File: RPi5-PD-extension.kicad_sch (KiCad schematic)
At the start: 4 parts, among them J1 HDMI0_Plug, J2 HDMI0_Receptacle, J3 HDMI1_Plug, J4 HDMI1_Receptacle

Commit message: Design v1
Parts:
- added C1, C13, C2: 10uF, symbol Device:C
- added C10, C7, C8, C9: 10nF, symbol Device:C
- added C11, C12, C21, C22, C23, C24, C25, C27, C28: 22uF, symbol Device:C
- added C14, C15, C29: 1uF, symbol Device:C
- added C16, C17, C3, C4: 330pF, symbol Device:C
- added C18, C20, C26: 100nF, symbol Device:C
- added C19: 22nF, symbol Device:C
- added C5, C6: 4.7uF, symbol Device:C
- added D1: BZT52C18, Diode_SMD:D_SOD-123F, symbol Diode:BZT52Bxx
- added J5: USB_C_PD_Receptacle, symbol Connector:USB_C_Receptacle_PowerOnly_6P
- added L1: 2.2uH, symbol Device:L
- added P1: USB_C_5V5A_Plug, symbol Connector:USB_C_Receptacle_USB2.0_14P
- added Q1: XR100P04, Package_TO_SOT_SMD:TO-252-2, symbol Transistor_FET:SUD50P04-08
- added R1, R2, R3, R5, R6: 10k, symbol Device:R
- added R10, R4: 220k, symbol Device:R
- added R11: 30k, symbol Device:R
- added R12: 330k, symbol Device:R
- added R13, R14, R7: 51k, symbol Device:R
- added R15: 1k, symbol Device:R
- added R8: 10m 1%, symbol Device:R
- added R9: 0, symbol Device:R
- added TP1: SWC, symbol Connector:TestPoint
- added TP2: GND, symbol Connector:TestPoint
- added TP3: VDD, symbol Connector:TestPoint
- added TP4: SWD, symbol Connector:TestPoint
- added U1: TPS25730D, Package_DFN_QFN:Texas_REF0038A_WQFN-38-2EP_6x4mm_P0.4, symbol Interface_USB:TPS25730D
- added U2: CYPD3175-24LQXQ, Package_DFN_QFN:QFN-24-1EP_4x4mm_P0.5mm_EP2.75x2.75mm, symbol Interface_USB:CYPD3175-24LQXQ
- added U4: TPS51396A, Package_DFN_QFN:Texas_RJE0020A_VQFN-20-1EP_3x3mm_P0.45mm_EP0.675x0.76mm, symbol Regulator_Switching:TPS51396A
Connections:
- new net: D1.2 (A), Q1.1 (G), R14.2, R15.1
- new net: C29.1, R12.1, U4.17 (VCC)
- new net: R12.2, R13.1, U4.15 (MODE)
- new net: R3.1, U1.26 (RESERVED)
- new net: C18.2, U4.1 (BST)
- new net: C19.1, U4.11 (SS)
- new net: C18.1, L1.1, U4.19 (SW), U4.20 (SW), U4.6 (SW)
- new net: C26.1, C27.1, C28.1, U4.2 (VIN), U4.3 (VIN), U4.4 (VIN), U4.5 (VIN)
- new net: C11.1, C12.1, C13.1, U1.20 (PPHV)
- new net: U1.15 (DRAIN), U1.30 (DRAIN), U1.40 (DRAIN)
- new net: R2.1, U1.27 (RESERVED)
- new net: R1.1, U1.36 (RESERVED)
- new net: C5.1, U1.4 (LDO_1V5)
- new net: R8.1, U2.19 (CSP)
- new net: C14.1, U2.24 (VCCD)
- new net: J5.S1 (SHIELD), R9.1
- new net ADC_LV1: R4.2, R5.1, U1.2 (ADCIN1)
- new net ADC_LV3: R6.2, R7.1, U1.5 (ADCIN3), U1.7 (ADCIN4)
- new net CC1: C3.1, J5.A5 (CC1), U1.28 (CC1)
- new net CC2: C4.1, J5.B5 (CC2), U1.29 (CC2)
- new net CCS_SWC: TP1.1, U2.8 (P0.1/SWD_CLK_0)
- new net CCS_SWD: TP4.1, U2.7 (P0.0/SWD_DAT_0)
- new net CCS_VDD: C15.1, TP3.1, U2.23 (VDDD)
- new net D+: P1.A6 (D+), P1.B6 (D+), U2.17 (DP0/P3.0)
- new net D-: P1.A7 (D-), P1.B7 (D-), U2.16 (DM0/P3.1)
- new net EN: U4.12 (EN)
- new net FB: R10.2, R11.1, U2.20 (FB), U4.14 (FB)
- new net GND: C1.1, C1.2, C10.2, C11.2, C12.2, C13.2, C14.2, C15.2, C16.2, C17.2, C19.2, C2.2, C20.2, C21.2, C22.2, C23.2, C24.2, C25.2, C26.2, C27.2, C28.2, C29.2, C3.2, C4.2, C5.2, C6.2, C7.2, C8.2, C9.2, J5.A12 (GND), J5.B12 (GND), P1.A1 (GND), P1.A12 (GND), P1.B1 (GND), P1.B12 (GND), P1.S1 (SHIELD), R1.2, R11.2, R13.2, R2.2, R3.2, R5.2, R7.2, R8.2, R9.2, TP2.1, U1.11 (GND), U1.12 (GND), U1.14 (GND), U1.16 (GND), U1.17 (GND), U1.31 (GND), U1.34 (GND), U1.38 (VIN_3V3), U1.39 (GND), U1.8 (I2Ct_SDA), U1.9 (I2Ct_SCL), U2.22 (GND), U2.25 (GND), U4.10 (NC), U4.13 (AGND), U4.16 (NC), U4.18 (GND), U4.21 (GND), U4.7 (GND), U4.8 (GND)
- new net LDO_3V3: C2.1, R4.1, R6.1, U1.1 (LDO_3V3), U1.3 (ADCIN2)
- new net PCTRL: R15.2, U2.3 (VBUS_P_CTRL)
- new net PG: U4.9 (PGOOD)
- new net SCC1: C17.1, P1.A5 (CC1), U2.15 (CC1)
- new net SCC2: C16.1, P1.B5 (CC2), U2.14 (CC2)
- new net VBUS: C10.1, C6.1, C7.1, C8.1, C9.1, D1.1 (K), J5.A9 (VBUS), J5.B9 (VBUS), Q1.3 (S), R14.1, U1.23 (VBUS_IN), U1.32 (VBUS), U2.18 (VBUS_IN_DIS)
- new net VOUT: C20.1, C21.1, C22.1, C23.1, C24.1, C25.1, L1.2, P1.A4 (VBUS), P1.A9 (VBUS), P1.B4 (VBUS), P1.B9 (VBUS), Q1.2 (D), R10.1, U2.11 (VBUS_C_MON_DIS)
- new net ~{SINK_EN}: U1.19 (~{SINK_EN})
- no-connect marks 0 -> 15
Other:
- note added: "2026/01/09"
- note added: "CYPD3175 USB-C PD Source Controller"
- note added: "Configured to negotiate 9V+ 3A+"
- note added: "Raspberry Pi 5 USB PD to 5V 5A Extension Card"
- note added: "Status LED"
- note added: "TPS25730D USB-C PD Sink Controller"
- note added: "TPS51396A 5V 8A Output Buck Converter"
- note added: "USB 2.0 Data Transfer is not possible."
- note added: "USB-C PD Receptacle & 5V5A Plug"
- note added: "Will be configured to negotiate 5V 5A"
- note added: "v1_unreviewed"
- moved on the sheet: J1, J2, J3, J4

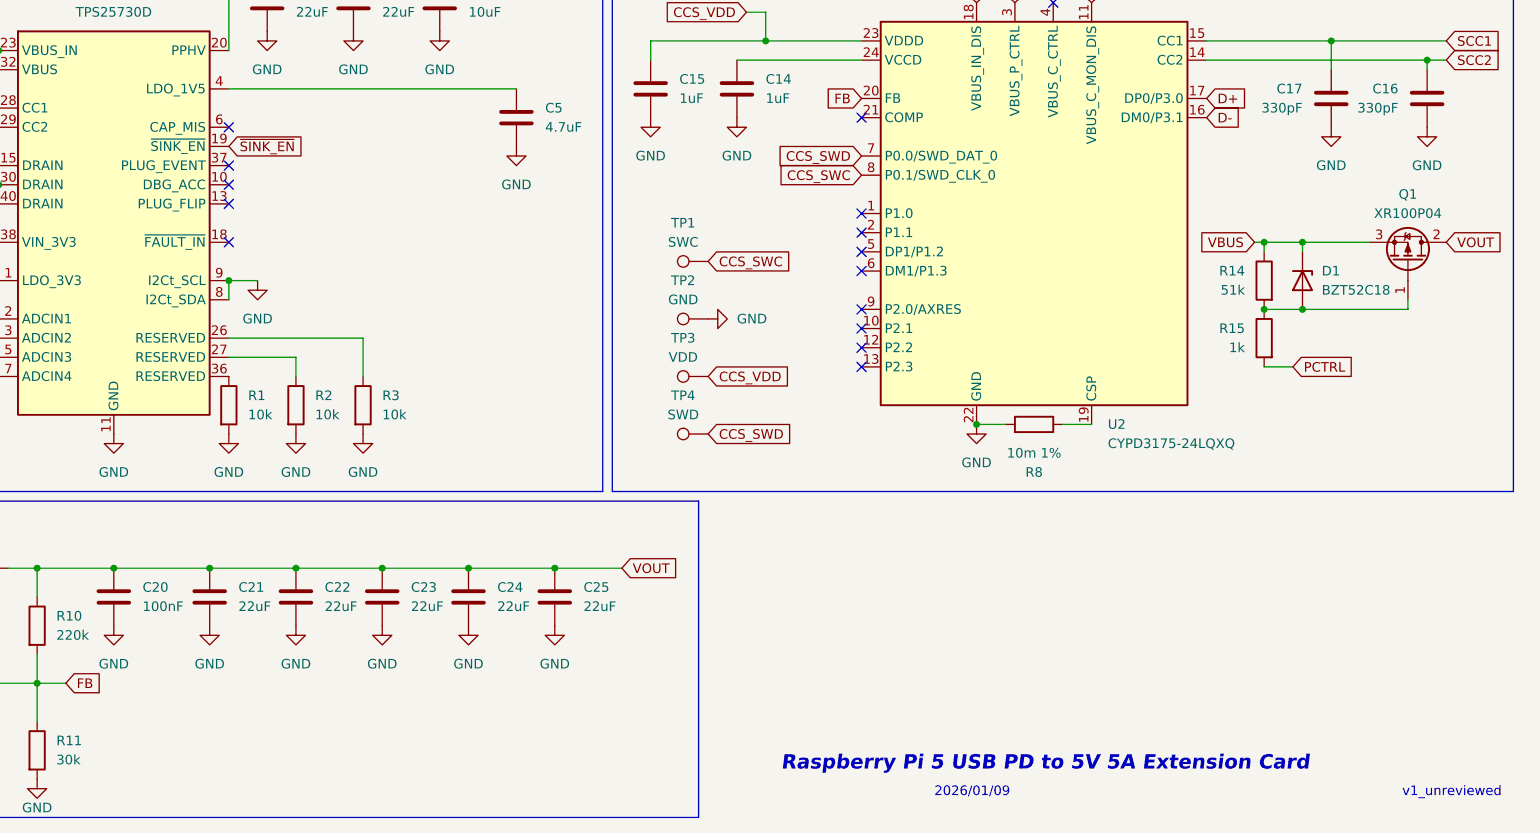
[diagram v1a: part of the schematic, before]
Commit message: EN pin on buck converter connected to LDO
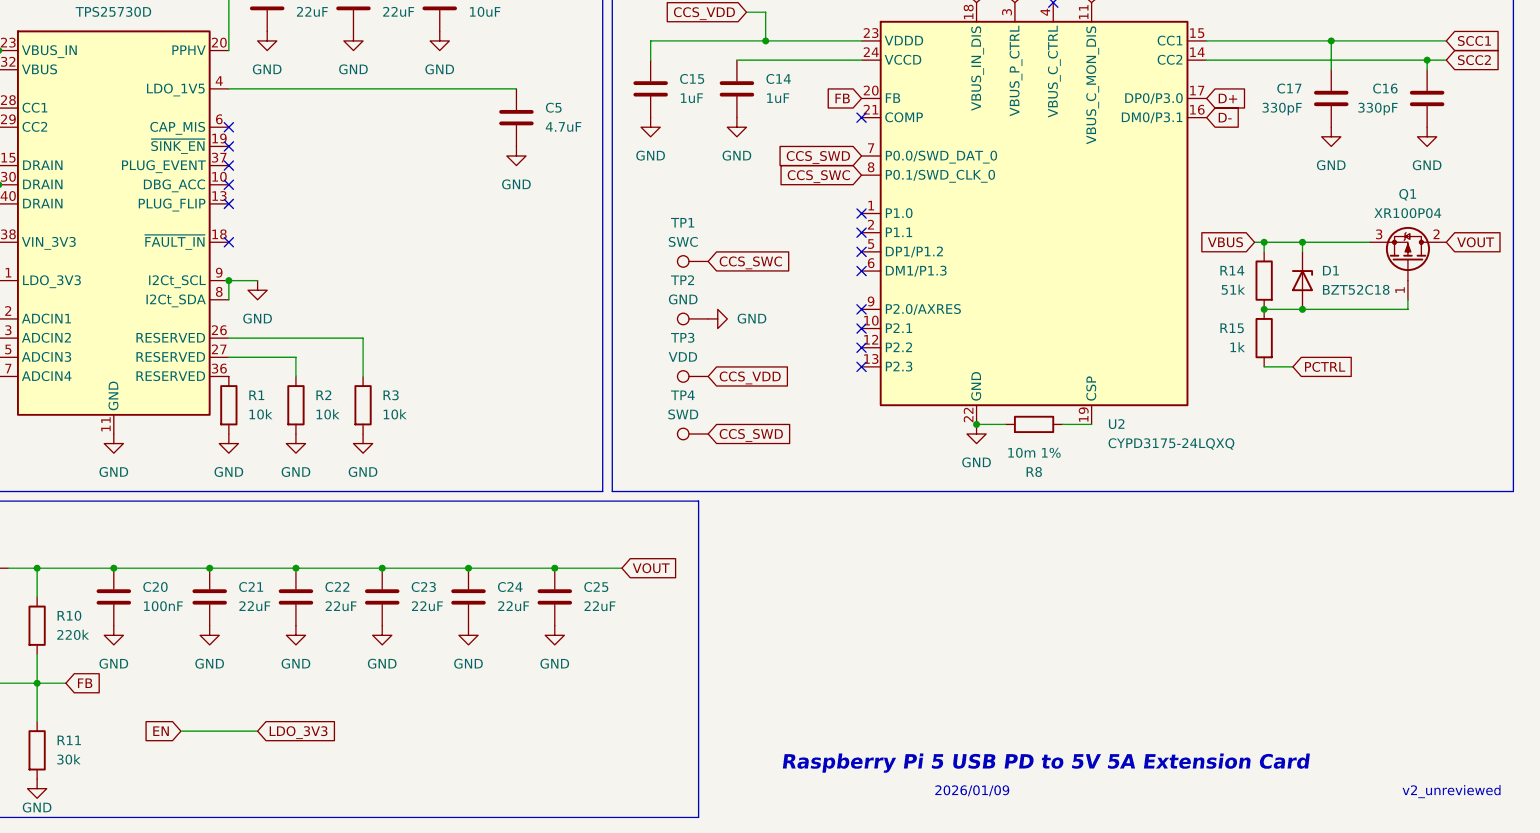
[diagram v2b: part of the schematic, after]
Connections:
- net LDO_3V3 is gone; now on net EN: C2.1, R4.1, R6.1, U1.1 (LDO_3V3), U1.3 (ADCIN2)
- net ~{SINK_EN}: no longer names the net of U1.19 (~{SINK_EN})
- no-connect marks 15 -> 16
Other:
- note added: "v2_unreviewed"
- note removed: "v1_unreviewed"
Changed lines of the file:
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@@
 		)
 	)
-	(text "v1_unreviewed"
+	(text "v2_unreviewed"
 		(exclude_from_sim no)
 		(at 268.478 193.548 0)
@@
 	)
 	(no_connect
+		(at 113.03 107.95)
+	)
+	(no_connect
 		(at 113.03 113.03)
 	)
@@
 	(wire
 		(pts
+			(xy 116.84 185.42) (xy 106.68 185.42)
+		)
+		(stroke
+			(width 0)
+			(type default)
+		)
+	)
+	(wire
+		(pts
 			(xy 97.79 163.83) (xy 110.49 163.83)
 		)
@@
 		)
 	)
+	(global_label "EN"
+		(shape input)
+		(at 106.68 185.42 180)
+		(fields_autoplaced yes)
+		(effects
+			(font
+				(size 1.27 1.27)
+			)
+			(justify right)
+		)
+		(property "Intersheetrefs" "${INTERSHEET_REFS}"
+			(at 101.2153 185.42 0)
+			(effects
+				(font
+					(size 1.27 1.27)
+				)
+				(justify right)
+				(hide yes)
+			)
+		)
+	)
 	(global_label "LDO_3V3"
 		(shape input)
@@
 		)
 	)
+	(global_label "LDO_3V3"
+		(shape input)
+		(at 116.84 185.42 0)
+		(fields_autoplaced yes)
+		(effects
+			(font
+				(size 1.27 1.27)
+				(thickness 0.1588)
+			)
+			(justify left)
+		)
+		(property "Intersheetrefs" "${INTERSHEET_REFS}"
+			(at 127.929 185.42 0)
+			(effects
+				(font
+					(size 1.27 1.27)
+				)
+				(justify left)
+				(hide yes)
+			)
+		)
+	)
 	(global_label "CC2"
 		(shape input)
@@
 			(effects
 				(font
-					(size 1.27 1.27)
-				)
-				(justify left)
-				(hide yes)
-			)
-		)
-	)
-	(global_label "~{SINK_EN}"
-		(shape input)
-		(at 113.03 107.95 0)
-		(fields_autoplaced yes)
-		(effects
-			(font
-				(size 1.27 1.27)
-			)
-			(justify left)
-		)
-		(property "Intersheetrefs" "${INTERSHEET_REFS}"
-			(at 123.8771 107.95 0)
-			(effects
-				(font
